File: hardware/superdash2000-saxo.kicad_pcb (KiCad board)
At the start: 2 copper layers, 76.2 x 55.9 mm, 21 parts, among them IC1 MAX4617CPE+, J1 Molex 34691-0161, U1 L7805, U2 TLV2372

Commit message: hardware: Update pcb
Signed-off-by: Thomas Antonini <antonini.thomas@gmail.com>
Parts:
- moved R4 43.6 mm to (64.1, 58.4), turned to 180 degrees
- moved R7 43.2 mm to (45.1, 63.5)
- moved R8 43.2 mm to (56.5, 63.5)
- moved R3 43.2 mm to (45.1, 58.4)
- moved U2 43.2 mm to (40.6, 57.1)
- moved RV2 31.9 mm to (90.8, 104.1)
- moved R9 31.9 mm to (67.9, 95.9)
- moved IC1 31.9 mm to (51.4, 99.7), turned to -90 degrees
- moved C3 31.8 mm to (63.4, 95.9)
- moved JP1 31.4 mm to (73.6, 74.9), turned to 180 degrees
- moved R5 30.5 mm to (57.1, 106.0)
- moved R6 30.5 mm to (57.1, 101.6)
- moved U1 28.6 mm to (64.1, 89.0)
- moved F1 25.0 mm to (61.6, 72.4), turned to 0 degrees
- moved C1 24.5 mm to (63.5, 81.3), turned to 180 degrees
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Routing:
- net +5V: track 0.00 -> 75.2 mm
- net VCC: track 0.00 -> 43.8 mm
- net /WATER_TEMP: track 0.00 -> 43.3 mm
- net /DIMMER: track 0.00 -> 43.3 mm
- net /VIN: track 0.00 -> 33.6 mm
- net Net-(C1-Pad1): track 0.00 -> 23.8 mm
- net /A0: track 0.00 -> 18.3 mm
- net Net-(R7-Pad1): track 0.00 -> 12.2 mm
- net +BATT: track 0.00 -> 8.44 mm
- net Net-(R3-Pad1): track 0.00 -> 7.50 mm
- net /LCD_BRIGHTNESS+: track 0.00 -> 4.45 mm
- net /D3: track 0.00 -> 3.82 mm
- net /D4: track 0.00 -> 3.81 mm
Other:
- board size 76.2 x 55.9 mm -> 67.3 x 55.9 mm

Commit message: hardware: Update pcb
Signed-off-by: Thomas Antonini <antonini.thomas@gmail.com>
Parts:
- moved RV2 6.85 mm to (84.5, 101.6), turned to 90 degrees
- moved RV1 4.07 mm to (73.7, 101.6), turned to 90 degrees
- moved C3 2.47 mm to (61.0, 95.9), turned to 0 degrees
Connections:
- net /D2 renamed /BUTTON+
- J1 pad 12: /LCD_BRIGHTNESS+ -> /LCD_BRIGHTNESS-
- J1 pad 4: /LCD_BRIGHTNESS- -> /LCD_BRIGHTNESS+
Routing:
- net /BUTTON+: track 0.00 -> 72.0 mm
- net /LCD_BRIGHTNESS+: track 4.45 -> 34.4 mm
- net /LCD_BRIGHTNESS-: track 0.00 -> 22.8 mm
- net Net-(IC1-Pad14): track 0.00 -> 16.2 mm
- net Net-(IC1-Pad15): track 0.00 -> 8.80 mm

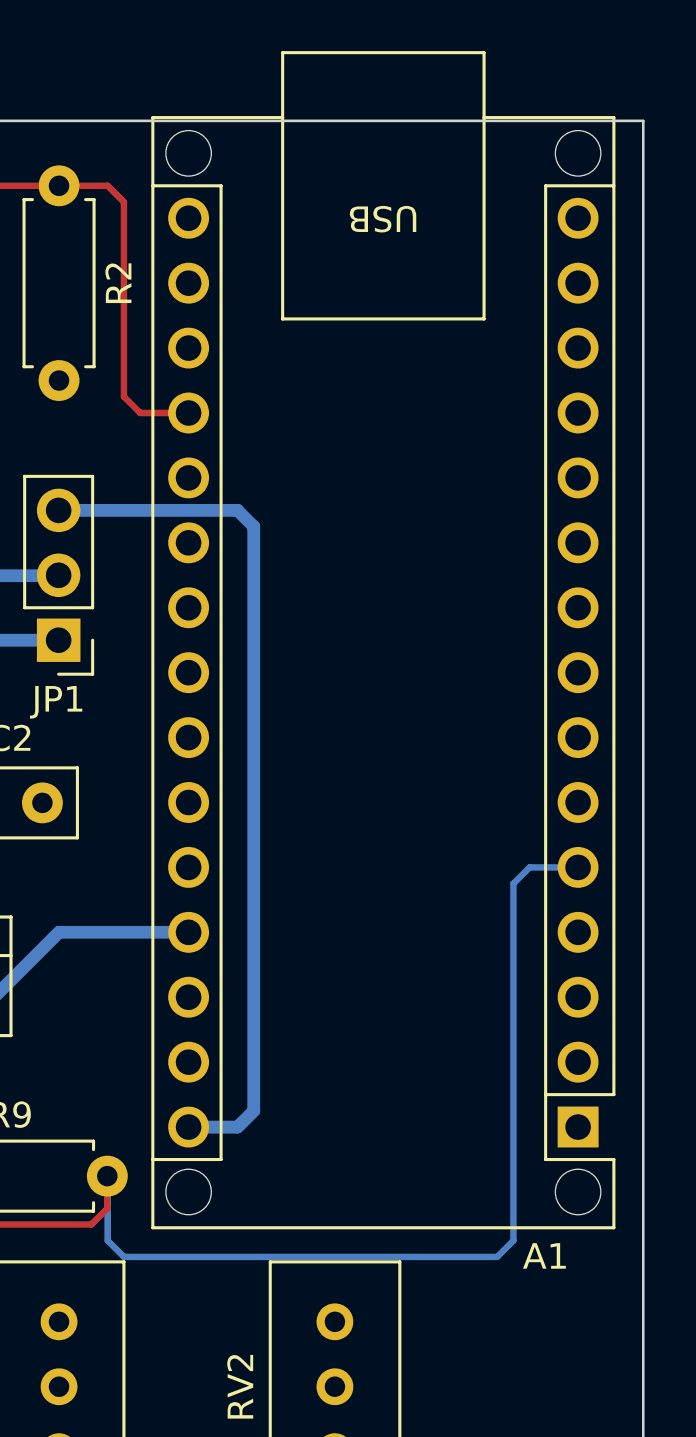
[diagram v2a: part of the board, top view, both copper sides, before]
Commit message: hardware: Change arduino footprint to without holes
Signed-off-by: Thomas Antonini <antonini.thomas@gmail.com>
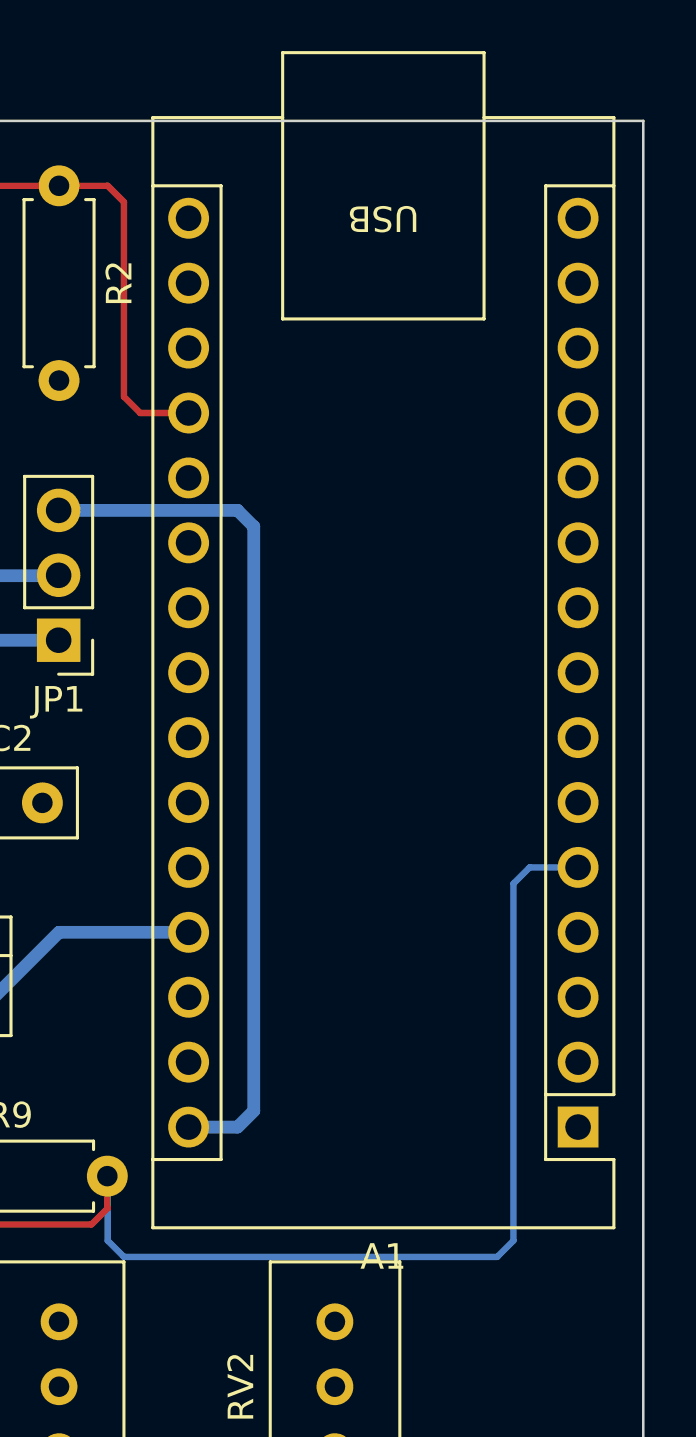
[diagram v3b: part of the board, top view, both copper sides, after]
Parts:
- A1: footprint Arduino_Nano_Every:Arduino_Nano_Every_WithMountingHoles -> Arduino_Nano_Every:Arduino_Nano_Every
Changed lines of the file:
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@@
     )
   )
-  (footprint "Arduino_Nano_Every:Arduino_Nano_Every_WithMountingHoles" (layer "F.Cu")
+  (footprint "Arduino_Nano_Every:Arduino_Nano_Every" (layer "F.Cu")
     (at 93.97 93.98 180)
     (descr "Arduino Nano Every, http://www.mouser.com/pdfdocs/Gravitech_Arduino_Nano3_0.pdf")
@@
     (property "Sheetname" "")
     (attr through_hole)
-    (fp_text reference "A1" (at 1.26 -5.08 180) (layer "F.SilkS")
+    (fp_text reference "A1" (at 7.62 -5.08 180) (layer "F.SilkS")
       (effects (font (size 1 1) (thickness 0.15)))
     )
-    (fp_text value "Arduino_Nano_Every" (at 8.89 15.24 270) (layer "F.Fab")
+    (fp_text value "Arduino_Nano_Every" (at 8.89 19.05 270) (layer "F.Fab")
       (effects (font (size 1 1) (thickness 0.15)))
     )
@@
       (effects (font (size 1 1) (thickness 0.15)))
     )
-    (fp_text user "${REFERENCE}" (at 6.35 16.51 270) (layer "F.Fab")
+    (fp_text user "${REFERENCE}" (at 6.35 19.05 270) (layer "F.Fab")
       (effects (font (size 1 1) (thickness 0.15)))
     )
+    (fp_line (start 11.56 42.04) (end 3.68 42.04) (layer "F.SilkS") (width 0.12))
+    (fp_line (start 1.27 -1.27) (end -1.4 -1.27) (layer "F.SilkS") (width 0.12))
+    (fp_line (start 1.27 36.83) (end -1.4 36.83) (layer "F.SilkS") (width 0.12))
+    (fp_line (start -1.4 39.5) (end 3.68 39.5) (layer "F.SilkS") (width 0.12))
+    (fp_line (start 13.97 36.83) (end 16.64 36.83) (layer "F.SilkS") (width 0.12))
+    (fp_line (start 16.64 -3.94) (end -1.4 -3.94) (layer "F.SilkS") (width 0.12))
+    (fp_line (start 1.27 1.27) (end 1.27 -1.27) (layer "F.SilkS") (width 0.12))
+    (fp_line (start 1.27 1.27) (end 1.27 36.83) (layer "F.SilkS") (width 0.12))
+    (fp_line (start -1.4 1.27) (end -1.4 39.5) (layer "F.SilkS") (width 0.12))
+    (fp_line (start 16.64 39.5) (end 16.64 -3.94) (layer "F.SilkS") (width 0.12))
+    (fp_line (start 3.68 31.62) (end 11.56 31.62) (layer "F.SilkS") (width 0.12))
+    (fp_line (start 11.56 31.62) (end 11.56 42.04) (layer "F.SilkS") (width 0.12))
+    (fp_line (start 13.97 -1.27) (end 13.97 36.83) (layer "F.SilkS") (width 0.12))
+    (fp_line (start 16.64 39.5) (end 11.56 39.5) (layer "F.SilkS") (width 0.12))
     (fp_line (start 1.27 1.27) (end -1.4 1.27) (layer "F.SilkS") (width 0.12))
-    (fp_line (start 13.97 36.83) (end 16.64 36.83) (layer "F.SilkS") (width 0.12))
-    (fp_line (start -1.4 1.27) (end -1.4 39.5) (layer "F.SilkS") (width 0.12))
-    (fp_line (start 13.97 -1.27) (end 13.97 36.83) (layer "F.SilkS") (width 0.12))
-    (fp_line (start 16.64 -3.94) (end -1.4 -3.94) (layer "F.SilkS") (width 0.12))
+    (fp_line (start -1.4 -3.94) (end -1.4 -1.27) (layer "F.SilkS") (width 0.12))
     (fp_line (start 13.97 -1.27) (end 16.64 -1.27) (layer "F.SilkS") (width 0.12))
-    (fp_line (start 16.64 39.5) (end 16.64 -3.94) (layer "F.SilkS") (width 0.12))
     (fp_line (start 3.68 42.04) (end 3.68 31.62) (layer "F.SilkS") (width 0.12))
-    (fp_line (start -1.4 39.5) (end 3.68 39.5) (layer "F.SilkS") (width 0.12))
-    (fp_line (start 1.27 1.27) (end 1.27 36.83) (layer "F.SilkS") (width 0.12))
-    (fp_line (start 16.64 39.5) (end 11.56 39.5) (layer "F.SilkS") (width 0.12))
-    (fp_line (start 3.68 31.62) (end 11.56 31.62) (layer "F.SilkS") (width 0.12))
-    (fp_line (start 11.56 42.04) (end 3.68 42.04) (layer "F.SilkS") (width 0.12))
-    (fp_line (start 11.56 31.62) (end 11.56 42.04) (layer "F.SilkS") (width 0.12))
-    (fp_line (start 1.27 36.83) (end -1.4 36.83) (layer "F.SilkS") (width 0.12))
-    (fp_line (start -1.4 -3.94) (end -1.4 -1.27) (layer "F.SilkS") (width 0.12))
-    (fp_line (start 1.27 -1.27) (end -1.4 -1.27) (layer "F.SilkS") (width 0.12))
-    (fp_line (start 1.27 1.27) (end 1.27 -1.27) (layer "F.SilkS") (width 0.12))
+    (fp_line (start 16.75 42.16) (end 16.75 -4.06) (layer "F.CrtYd") (width 0.05))
+    (fp_line (start 16.75 42.16) (end -1.53 42.16) (layer "F.CrtYd") (width 0.05))
     (fp_line (start -1.53 -4.06) (end 16.75 -4.06) (layer "F.CrtYd") (width 0.05))
     (fp_line (start -1.53 -4.06) (end -1.53 42.16) (layer "F.CrtYd") (width 0.05))
-    (fp_line (start 16.75 42.16) (end -1.53 42.16) (layer "F.CrtYd") (width 0.05))
-    (fp_line (start 16.75 42.16) (end 16.75 -4.06) (layer "F.CrtYd") (width 0.05))
+    (fp_line (start 11.43 31.75) (end 11.43 41.91) (layer "F.Fab") (width 0.1))
+    (fp_line (start -1.27 -2.54) (end 0 -3.81) (layer "F.Fab") (width 0.1))
+    (fp_line (start 16.51 39.37) (end -1.27 39.37) (layer "F.Fab") (width 0.1))
+    (fp_line (start 3.81 31.75) (end 11.43 31.75) (layer "F.Fab") (width 0.1))
     (fp_line (start -1.27 39.37) (end -1.27 -2.54) (layer "F.Fab") (width 0.1))
-    (fp_line (start 11.43 31.75) (end 11.43 41.91) (layer "F.Fab") (width 0.1))
+    (fp_line (start 16.51 -3.81) (end 16.51 39.37) (layer "F.Fab") (width 0.1))
+    (fp_line (start 11.43 41.91) (end 3.81 41.91) (layer "F.Fab") (width 0.1))
+    (fp_line (start 3.81 41.91) (end 3.81 31.75) (layer "F.Fab") (width 0.1))
     (fp_line (start 0 -3.81) (end 16.51 -3.81) (layer "F.Fab") (width 0.1))
-    (fp_line (start -1.27 -2.54) (end 0 -3.81) (layer "F.Fab") (width 0.1))
-    (fp_line (start 11.43 41.91) (end 3.81 41.91) (layer "F.Fab") (width 0.1))
-    (fp_line (start 16.51 39.37) (end -1.27 39.37) (layer "F.Fab") (width 0.1))
-    (fp_line (start 3.81 41.91) (end 3.81 31.75) (layer "F.Fab") (width 0.1))
-    (fp_line (start 16.51 -3.81) (end 16.51 39.37) (layer "F.Fab") (width 0.1))
-    (fp_line (start 3.81 31.75) (end 11.43 31.75) (layer "F.Fab") (width 0.1))
-    (pad "" np_thru_hole circle (at 0 -2.54 180) (size 1.78 1.78) (drill 1.78) (layers *.Cu *.Mask))
-    (pad "" np_thru_hole circle (at 15.24 38.1 180) (size 1.78 1.78) (drill 1.78) (layers *.Cu *.Mask))
-    (pad "" np_thru_hole circle (at 0 38.1 180) (size 1.78 1.78) (drill 1.78) (layers *.Cu *.Mask))
-    (pad "" np_thru_hole circle (at 15.24 -2.54 180) (size 1.78 1.78) (drill 1.78) (layers *.Cu *.Mask))
     (pad "1" thru_hole rect (at 0 0 180) (size 1.6 1.6) (drill 1) (layers *.Cu *.Mask)
       (net 1 "unconnected-(A1-Pad1)") (pinfunction "TX1") (pintype "bidirectional+no_connect"))

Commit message: hardare: Update pcb
Signed-off-by: Thomas Antonini <antonini.thomas@gmail.com>
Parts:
- moved RV1 11.9 mm to (84.5, 106.7), turned to -90 degrees
- moved RV2 11.9 mm to (73.7, 106.7), turned to -90 degrees
- moved R1 1.27 mm to (68.6, 66.0)
- moved R2 1.27 mm to (73.7, 58.4)
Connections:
- R3 pad 2: /D3 -> /D4
- R4 pad 2: /D3 -> /D4
- R7 pad 2: /D4 -> /D3
- R8 pad 1: /D4 -> /D3
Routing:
- net /D7: track 0.00 -> 92.8 mm
- net /D6: track 0.00 -> 87.4 mm
- net /D5: track 0.00 -> 82.3 mm
- net /D4: track 3.81 -> 60.1 mm
- net /D3: track 3.82 -> 59.0 mm
- net Net-(IC1-Pad13): track 0.00 -> 42.8 mm
- net /LCD_SCL: track 0.00 -> 36.8 mm
- net /LCD_SDA: track 0.00 -> 36.3 mm
- net Net-(IC1-Pad12): track 0.00 -> 34.2 mm
- net /LCD_BRIGHTNESS+: track 34.4 -> 54.8 mm
- net /LCD_BRIGHTNESS-: track 22.8 -> 30.8 mm
- net /WATER_TEMP: track 43.3 -> 50.7 mm
- net /BUTTON+: track 72.0 -> 69.4 mm
- net +5V: track 75.2 -> 73.0 mm
- net /DIMMER: track 43.3 -> 41.1 mm
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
